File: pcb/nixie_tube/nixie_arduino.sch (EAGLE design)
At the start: 6 parts, among them IC1 LM1117DT, J1 DCJ0202

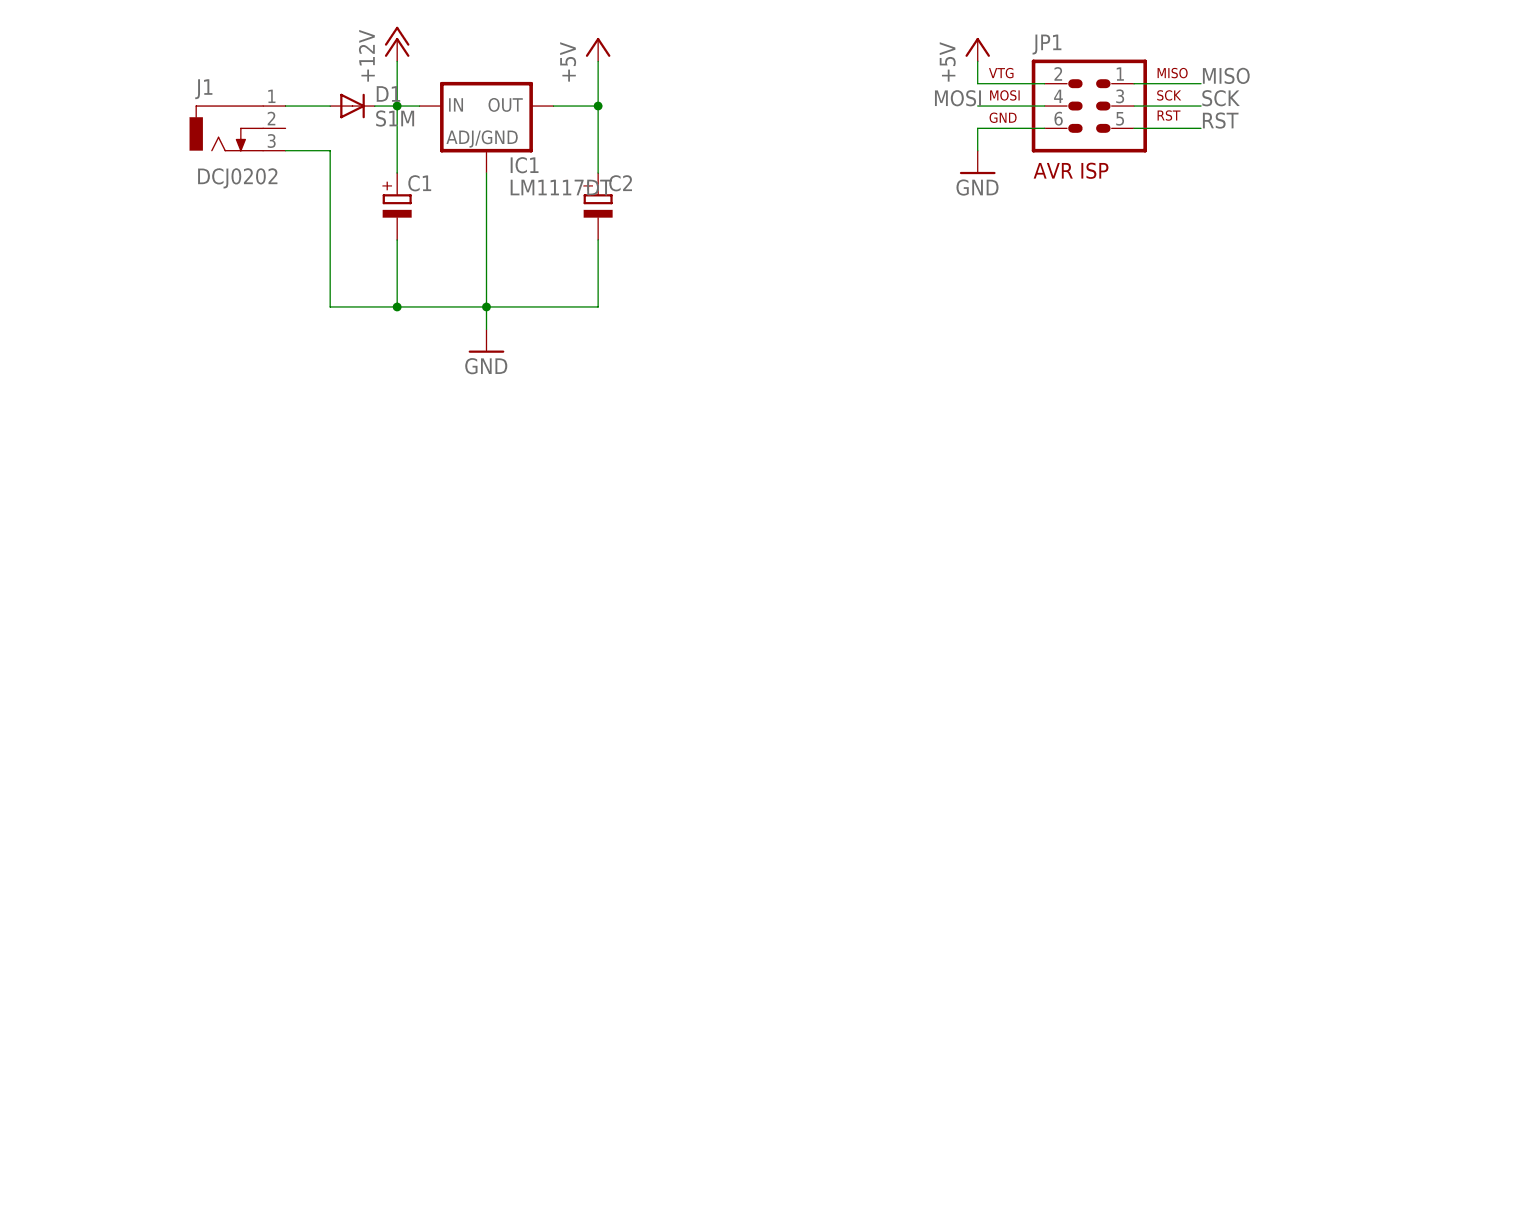
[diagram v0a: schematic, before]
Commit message: 
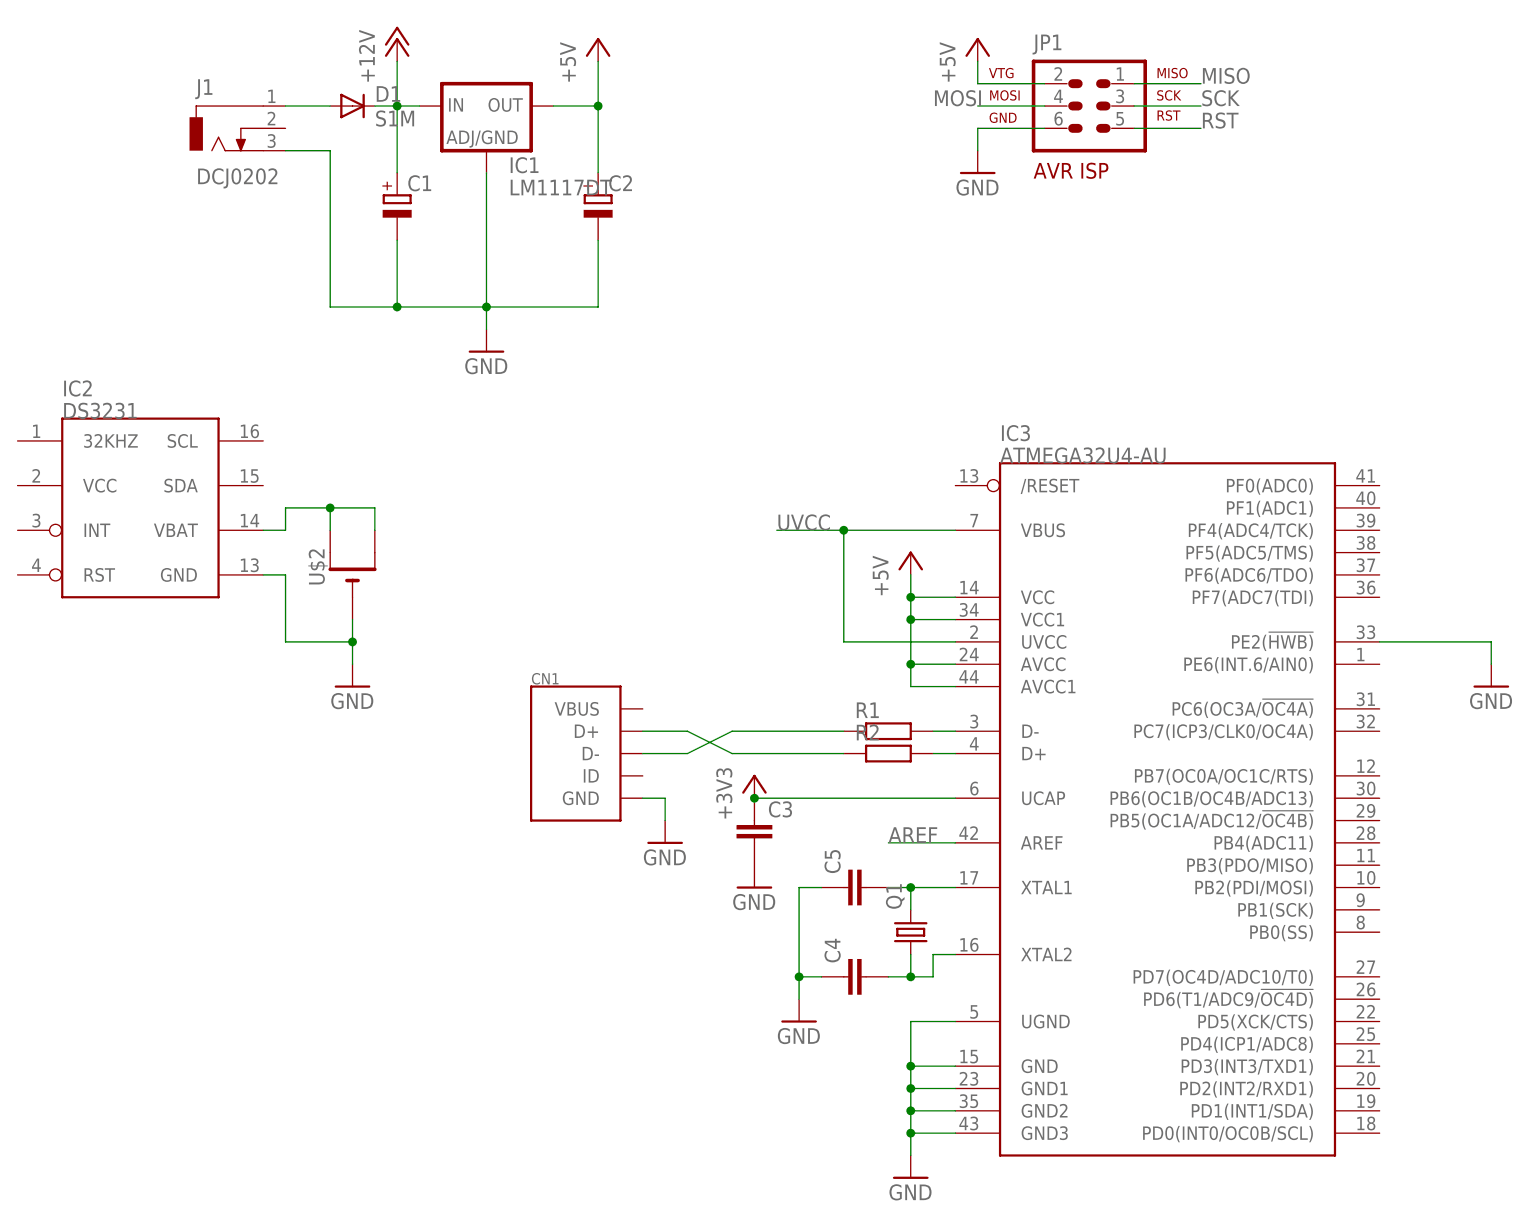
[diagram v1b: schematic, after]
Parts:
- added C3, C4, C5: (no value), nixie_tube:C-EUC0805K
- added CN1: (no value), nixie_tube:USBMINIB
- added IC2: DS3231, nixie_tube:DS3231
- added IC3: ATMEGA32U4-AU, nixie_tube:ATMEGA32U4-AU
- added Q1: (no value), nixie_tube:CRYSTALHC49UP
- added R1, R2: (no value), nixie_tube:R-EU_R0805
- added U$2: (no value), nixie_tube:CR1220SMT
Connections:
- new net +3V3: C3.1, IC3.UCAP
- new net AREF: IC3.AREF
- new net N$2: IC2.VBAT, U$2.+, U$2.+1
- new net N$3: IC3.D-, R1.2
- new net N$4: IC3.D+, R2.2
- new net N$5: CN1.D+, R2.1
- new net N$6: CN1.D-, R1.1
- new net N$8: C4.2, IC3.XTAL2, Q1.1
- new net N$9: C5.2, IC3.XTAL1, Q1.2
- new net UVCC: IC3.UVCC, IC3.VBUS
- net +5V: now also IC3.AVCC, IC3.AVCC1, IC3.VCC, IC3.VCC1
- net GND: now also C3.2, C4.1, C5.1, CN1.GND, IC2.GND, IC3.GND, IC3.GND1, IC3.GND2, IC3.GND3, IC3.PE2(!HWB), IC3.UGND, U$2.-
